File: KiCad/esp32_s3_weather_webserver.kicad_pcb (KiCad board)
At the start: 4 copper layers, 85 x 75 mm, 141 parts, among them IC201 MCP73831T-2ACI_OT, IC301 CP2102N-A02-GQFN28R, IC401 ESP32-S3-WROOM-1-N16R8, IC501 VEML7700-TT, IC502 DS3231MZ+TRL, J201 Barrel_Jack_Switch_Pin3Ring, J202 BM02B-GHS-TBT_LF__SN__N_, J301 USB_C_Receptacle_USB2.0, J302 USB_C_Receptacle_USB2.0, J401 Conn_01x04_Pin, J402 Conn_01x04_Pin, J403 Conn_01x04_Pin, J404 Conn_01x06_Pin, J405 TF-01A, Q201 DMG3415U-7, Q401 SS8050, Q402 SS8050, U201 AMS1117-3.3, U202 TLV62569DBV, U301 USBLC6-2SC6, U302 USBLC6-2SC6, U502 DS18B20, U503 LM35-LP, U504 DHT11

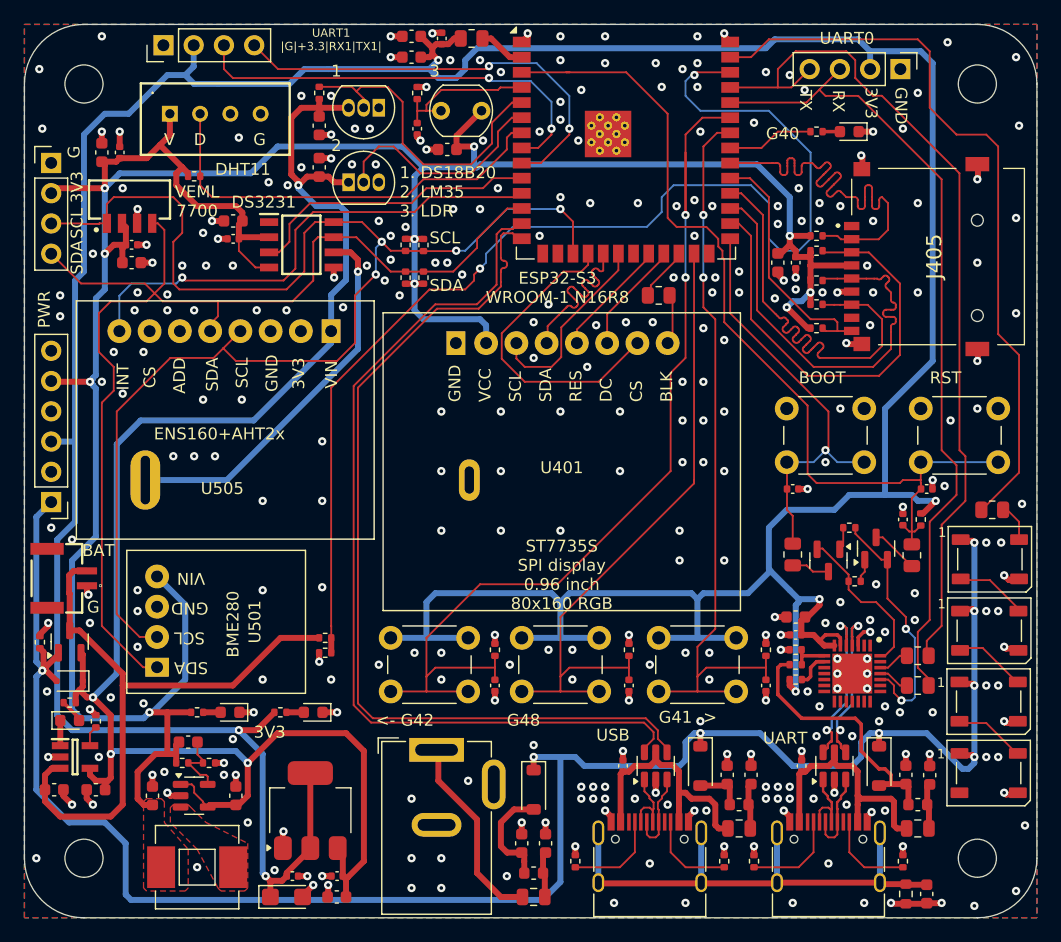
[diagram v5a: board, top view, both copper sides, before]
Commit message: Remove broken scheme parts
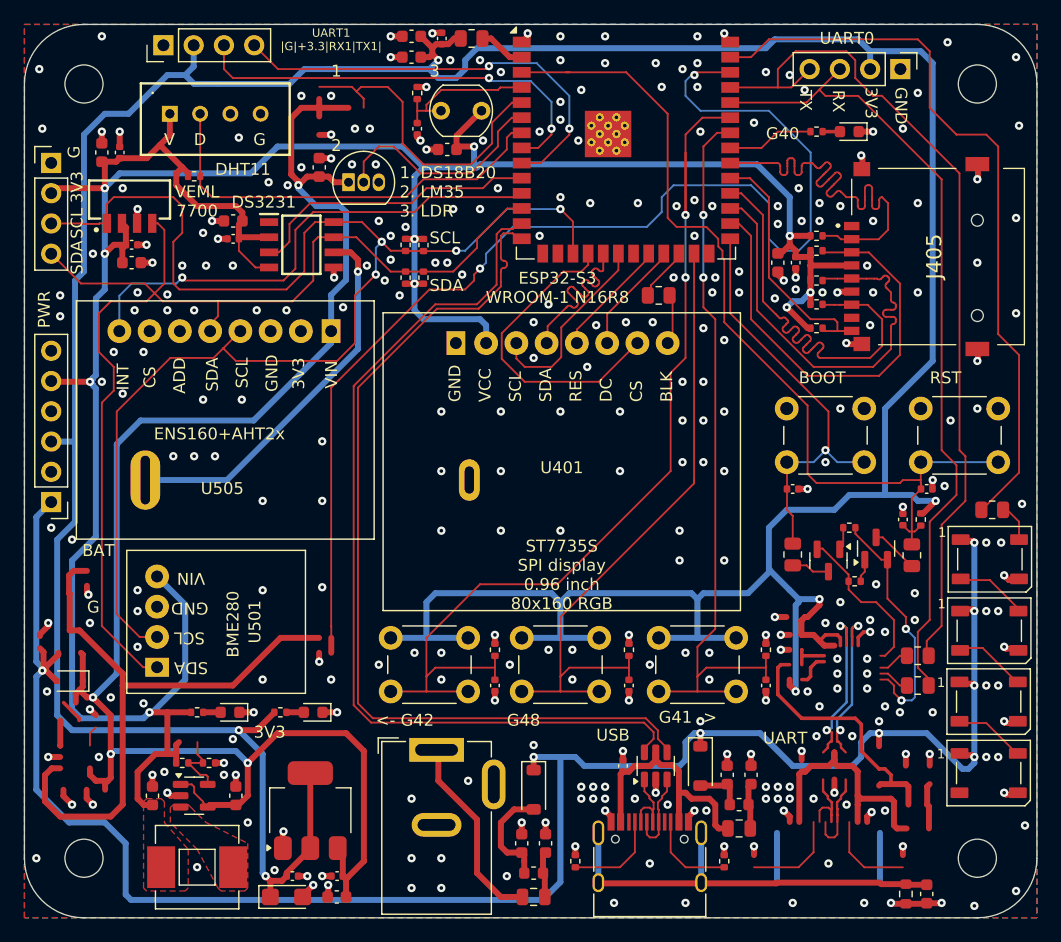
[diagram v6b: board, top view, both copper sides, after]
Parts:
- removed C207, C208: 2.2uF, Capacitor_SMD:C_0603_1608Metric
- removed C211: DNP, Capacitor_SMD:C_0603_1608Metric
- removed C214, C215: 22uF, Capacitor_SMD:C_0603_1608Metric
- removed C301: 4u7F, Capacitor_SMD:C_0603_1608Metric
- removed C302, C303: 100nF, Capacitor_SMD:C_0402_1005Metric
- removed C505: 10uF, Capacitor_SMD:C_0603_1608Metric
- removed D202: 1N5819HW-7-F, Diode_SMD:D_SOD-123
- removed D205: LED, LED_SMD:LED_0603_1608Metric
- removed F202: 3A, Fuse:Fuse_0805_2012Metric
- removed FB202: 120R, Fuse:Fuse_0603_1608Metric
- removed IC201: MCP73831T-2ACI_OT, esp32_s3_weather_webserver:SOT95P270X145-5N
- removed IC301: CP2102N-A02-GQFN28R, esp32_s3_weather_webserver:QFN50P500X500X80-29N-D
- removed J202: BM02B-GHS-TBT_LF__SN__N_, esp32_s3_weather_webserver:BM02B-GHS-TBT_1
- removed J301: USB_C_Receptacle_USB2.0, Connector_USB:USB_C_Receptacle_HRO_TYPE-C-31-M-12
- removed Q201: DMG3415U-7, Package_TO_SOT_SMD:SOT-23
- removed R203: 510R, Resistor_SMD:R_0402_1005Metric
- removed R204, R303, R304, R504: 5k1R, Resistor_SMD:R_0402_1005Metric
- removed R205, R210, R211: 100kR, Resistor_SMD:R_0402_1005Metric
- removed R301: 1kR, Resistor_SMD:R_0402_1005Metric
- removed R302: 22k1R, Resistor_SMD:R_0402_1005Metric
- removed R307: 47k5R, Resistor_SMD:R_0402_1005Metric
- removed U301: USBLC6-2SC6, Package_TO_SOT_SMD:SOT-23-6
- removed U502: DS18B20, Package_TO_SOT_THT:TO-92_Inline
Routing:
- net (no net): track 0.00 -> 171.5 mm, vias 0 -> 4
- net VBAT: track 52.6 -> 0.00 mm
- net USB2UART_VBUS: track 21.9 -> 0.00 mm
- net +VCC_USB2UART_FILT: track 21.8 -> 0.00 mm
- net /[3] USB/USB2UART_D-: track 14.9 -> 0.00 mm, vias 2 -> 0
- net /[3] USB/USB2UART_D+: track 14.5 -> 0.00 mm, vias 2 -> 0
- net /[3] USB/USB2UART_CONN_CC1: track 8.07 -> 0.00 mm
- net /[3] USB/USB2UART_CONN_CC2: track 7.57 -> 0.00 mm
- net /[3] USB/USB2UART_CONN_D+: track 7.21 -> 0.00 mm
- net /[3] USB/USB2UART_CONN_D-: track 7.03 -> 0.00 mm
- net +VCC_USB2UART_FUSE: track 3.88 -> 0.00 mm
- net /[3] USB/VBUS: track 3.14 -> 0.00 mm
- net /[3] USB/RSTB: track 2.95 -> 0.00 mm
- net /[2] Power/STAT: track 2.12 -> 0.00 mm
- net /[2] Power/LED_STAT_A: track 2.04 -> 0.00 mm
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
